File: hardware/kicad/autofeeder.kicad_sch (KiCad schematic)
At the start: 39 parts, among them J1 BATTERY, J2 MOTOR, J3 USB-C, J4 DBG, SW1_POWER1 Alps SKRPADE010, SW2_TIMER1 Alps SKRPADE010, SW3_MANUAL1 Alps SKRPADE010, SW4_SETTINGS1 Alps SKRPADE010, SW5_UP1 Alps SKRPADE010, SW6_DOWN1 Alps SKRPADE010, U1 ESP32-C6-Zero, U2 TP4056, U3 DW01A, U4 TPS63031DSKR, U5 DRV8871, U6 SN65HVD230, U8 FS8205A

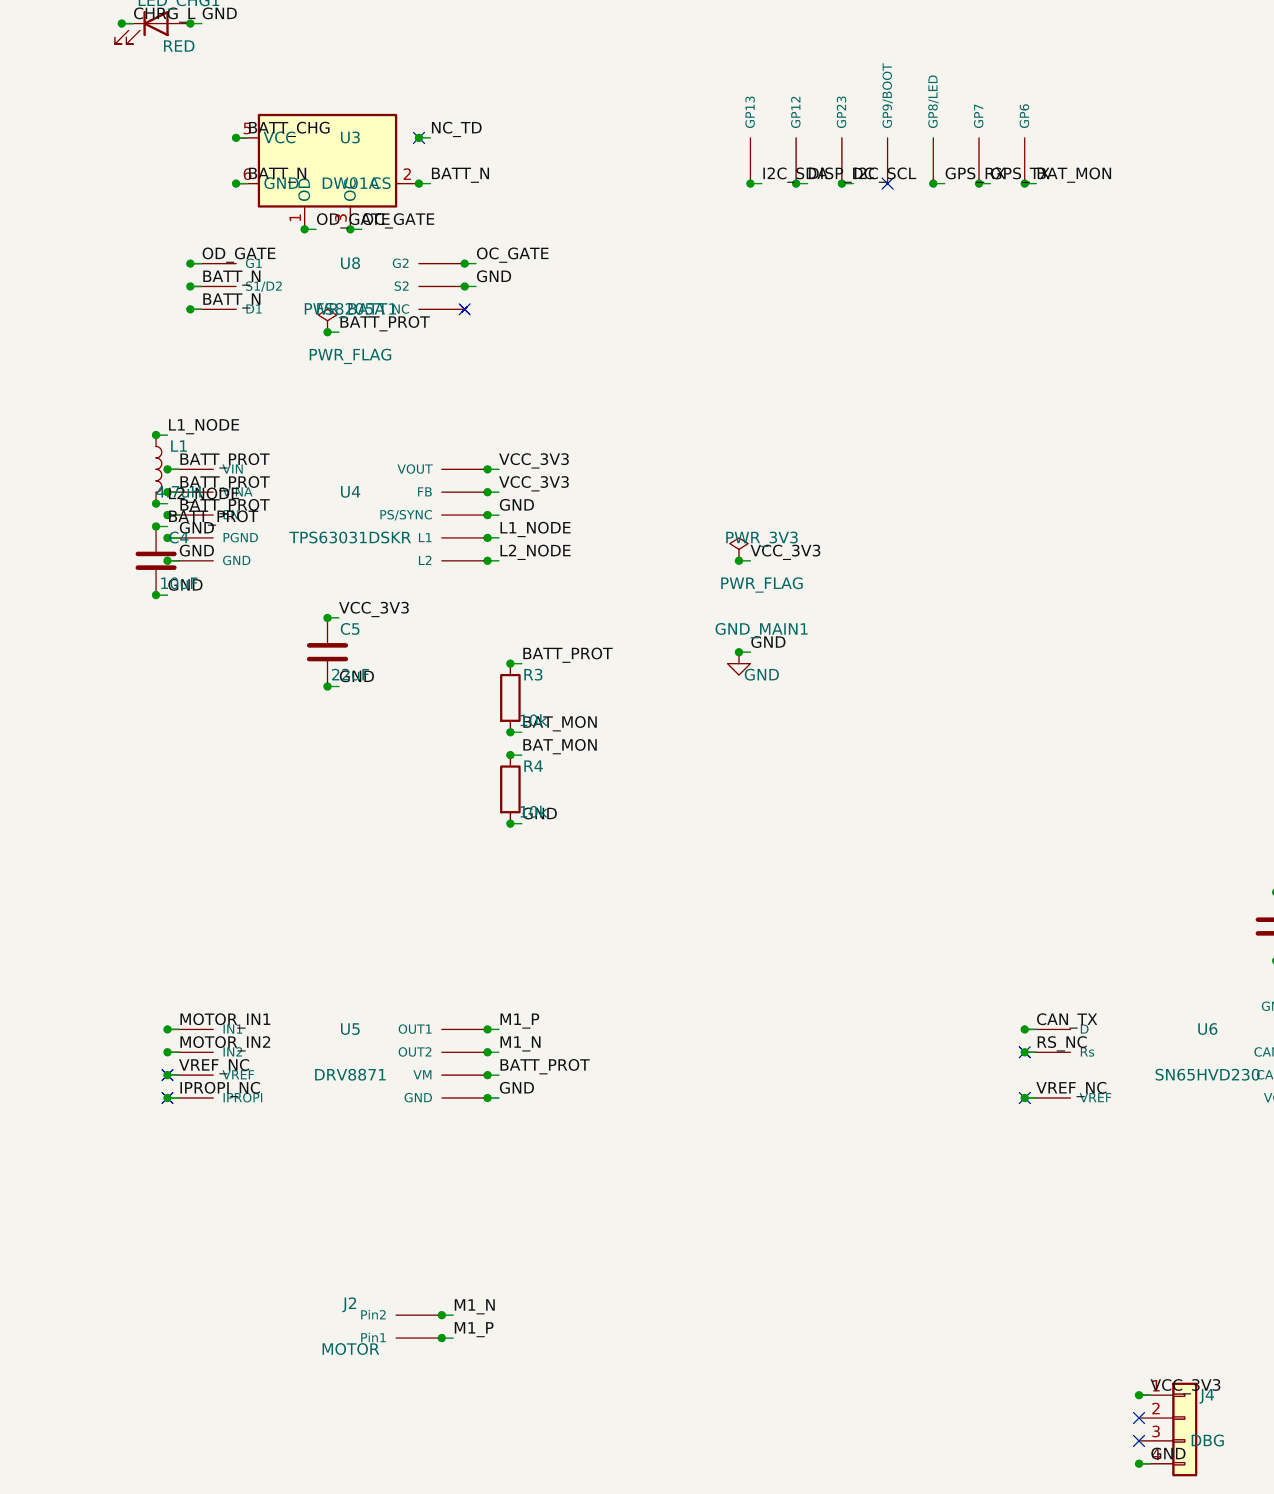
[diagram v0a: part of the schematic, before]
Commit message: Fix BATT_N unconnected net, migrate to 4-layer PCB, refresh fab outputs
- Add _pre_route_batt_n() to route BATT_N net (DW01A ↔ FS8205A protection ICs)
  via B.Cu segments + F.Cu through-via, eliminating the last unconnected net
- Update README power topology to include DW01A/FS8205A protection
- Update docs/bom.md: 2→4 layer count, remove stale bodge wire instructions,
  update DRC status to reflect 0 unconnected items
- Regenerate all fab outputs (gerbers, drill, BOM, CPL, DRC) for 4-layer board
- Add inner copper layers (In1.Cu, In2.Cu) to gerber set
- Add Wabo Labs logo footprint, display_sleep custom component
- Add MX1508 reference datasheets
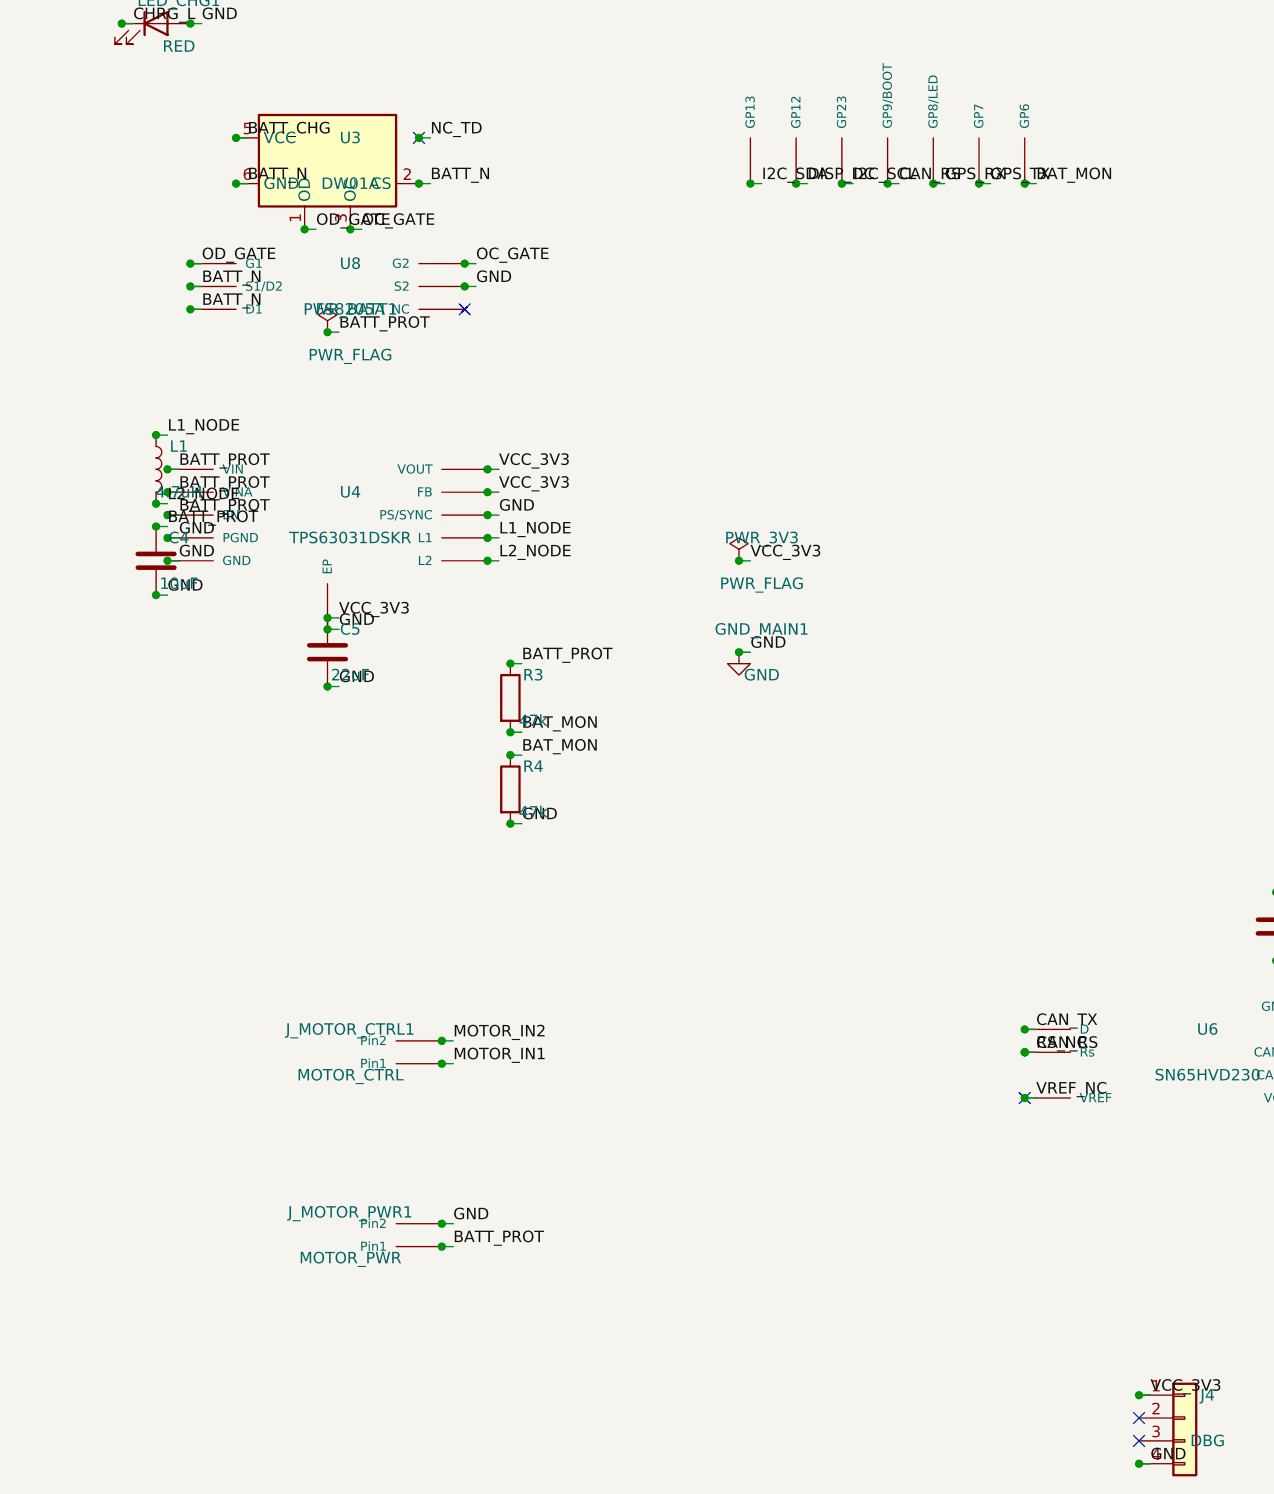
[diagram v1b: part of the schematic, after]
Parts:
- removed J2: MOTOR, Connector_JST:JST_XH_B2B-XH-A_1x02_P2.50mm_Vertical, symbol autofeeder:JST_XH_2P
- removed U5: DRV8871, Package_SO:SOIC-8_3.9x4.9mm_P1.27mm, symbol autofeeder:DRV8871
- added J_MOTOR_CTRL1: MOTOR_CTRL, Connector_JST:JST_XH_B2B-XH-A_1x02_P2.50mm_Vertical, symbol autofeeder:JST_XH_2P
- added J_MOTOR_PWR1: MOTOR_PWR, Connector_JST:JST_XH_B2B-XH-A_1x02_P2.50mm_Vertical, symbol autofeeder:JST_XH_2P
- R3, R4: value 10k -> 47k
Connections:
- net RS_NC is gone; now on net CAN_RS: U6.8 (Rs)
- net BATT_PROT: now also J_MOTOR_PWR1.1 (Pin1)
- net GND: now also U4.11 (EP), J_MOTOR_PWR1.2 (Pin2)
- net MOTOR_IN1: now also J_MOTOR_CTRL1.1 (Pin1)
- net MOTOR_IN2: now also J_MOTOR_CTRL1.2 (Pin2)
- net CAN_RS: now reaches U1.22 (GP9/BOOT)
- no-connect marks 16 -> 12
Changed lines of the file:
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@@
 	(junction (at 72.39 152.4) (diameter 0) (color 0 0 0 0))
 	(junction (at 72.39 154.94) (diameter 0) (color 0 0 0 0))
+	(junction (at 54.61 162.56) (diameter 0) (color 0 0 0 0))
 	(junction (at 35.56 140.97) (diameter 0) (color 0 0 0 0))
 	(junction (at 35.56 148.59) (diameter 0) (color 0 0 0 0))
@@
 	(junction (at 127 113.03) (diameter 0) (color 0 0 0 0))
 	(junction (at 121.92 113.03) (diameter 0) (color 0 0 0 0))
+	(junction (at 116.84 113.03) (diameter 0) (color 0 0 0 0))
 	(junction (at 144.78 55.88) (diameter 0) (color 0 0 0 0))
 	(junction (at 144.78 63.5) (diameter 0) (color 0 0 0 0))
 	(junction (at 144.78 66.04) (diameter 0) (color 0 0 0 0))
 	(junction (at 144.78 73.66) (diameter 0) (color 0 0 0 0))
-	(junction (at 36.83 207.01) (diameter 0) (color 0 0 0 0))
-	(junction (at 36.83 209.55) (diameter 0) (color 0 0 0 0))
-	(junction (at 72.39 207.01) (diameter 0) (color 0 0 0 0))
-	(junction (at 72.39 209.55) (diameter 0) (color 0 0 0 0))
-	(junction (at 36.83 212.09) (diameter 0) (color 0 0 0 0))
-	(junction (at 36.83 214.63) (diameter 0) (color 0 0 0 0))
-	(junction (at 72.39 212.09) (diameter 0) (color 0 0 0 0))
-	(junction (at 72.39 214.63) (diameter 0) (color 0 0 0 0))
-	(junction (at 67.31 241.3) (diameter 0) (color 0 0 0 0))
-	(junction (at 67.31 238.76) (diameter 0) (color 0 0 0 0))
+	(junction (at 67.31 210.82) (diameter 0) (color 0 0 0 0))
+	(junction (at 67.31 208.28) (diameter 0) (color 0 0 0 0))
+	(junction (at 67.31 231.14000000000001) (diameter 0) (color 0 0 0 0))
+	(junction (at 67.31 228.6) (diameter 0) (color 0 0 0 0))
 	(junction (at 132.08 207.01) (diameter 0) (color 0 0 0 0))
 	(junction (at 167.64000000000001 207.01) (diameter 0) (color 0 0 0 0))
@@
 	(junction (at 167.64000000000001 214.63) (diameter 0) (color 0 0 0 0))
 	(junction (at 167.64000000000001 204.47) (diameter 0) (color 0 0 0 0))
+	(junction (at 132.08 209.55) (diameter 0) (color 0 0 0 0))
 	(junction (at 170.18 205.74) (diameter 0) (color 0 0 0 0))
 	(junction (at 170.18 213.36) (diameter 0) (color 0 0 0 0))
@@
 	(no_connect (at 144.78 59.69))
 	(no_connect (at 144.78 62.230000000000004))
-	(no_connect (at 116.84 113.03))
-	(no_connect (at 36.83 212.09))
-	(no_connect (at 36.83 214.63))
 	(no_connect (at 132.08 214.63))
-	(no_connect (at 132.08 209.55))
 	(no_connect (at 144.78 250.19))
 	(no_connect (at 144.78 252.73))
@@
 	)
 	(wire
+		(pts (xy 54.61 162.56) (xy 55.88 162.56))
+		(stroke (width 0) (type solid))
+	)
+	(wire
 		(pts (xy 35.56 140.97) (xy 36.83 140.97))
 		(stroke (width 0) (type solid))
@@
 	)
 	(wire
+		(pts (xy 116.84 113.03) (xy 118.11 113.03))
+		(stroke (width 0) (type solid))
+	)
+	(wire
 		(pts (xy 144.78 55.88) (xy 146.05 55.88))
 		(stroke (width 0) (type solid))
@@
 	)
 	(wire
-		(pts (xy 36.83 207.01) (xy 38.1 207.01))
-		(stroke (width 0) (type solid))
-	)
-	(wire
-		(pts (xy 36.83 209.55) (xy 38.1 209.55))
-		(stroke (width 0) (type solid))
-	)
-	(wire
-		(pts (xy 72.39 207.01) (xy 73.66 207.01))
-		(stroke (width 0) (type solid))
-	)
-	(wire
-		(pts (xy 72.39 209.55) (xy 73.66 209.55))
-		(stroke (width 0) (type solid))
-	)
-	(wire
-		(pts (xy 36.83 212.09) (xy 38.1 212.09))
-		(stroke (width 0) (type solid))
-	)
-	(wire
-		(pts (xy 36.83 214.63) (xy 38.1 214.63))
-		(stroke (width 0) (type solid))
-	)
-	(wire
-		(pts (xy 72.39 212.09) (xy 73.66 212.09))
-		(stroke (width 0) (type solid))
-	)
-	(wire
-		(pts (xy 72.39 214.63) (xy 73.66 214.63))
-		(stroke (width 0) (type solid))
-	)
-	(wire
-		(pts (xy 67.31 241.3) (xy 68.58 241.3))
-		(stroke (width 0) (type solid))
-	)
-	(wire
-		(pts (xy 67.31 238.76) (xy 68.58 238.76))
+		(pts (xy 67.31 210.82) (xy 68.58 210.82))
+		(stroke (width 0) (type solid))
+	)
+	(wire
+		(pts (xy 67.31 208.28) (xy 68.58 208.28))
+		(stroke (width 0) (type solid))
+	)
+	(wire
+		(pts (xy 67.31 231.14000000000001) (xy 68.58 231.14000000000001))
+		(stroke (width 0) (type solid))
+	)
+	(wire
+		(pts (xy 67.31 228.6) (xy 68.58 228.6))
 		(stroke (width 0) (type solid))
 	)
@@
 		)
 	)
+	(label "GND"
+		(at 55.88 162.56 0)
+		(effects
+			(font (size 1.27 1.27))
+			(justify left bottom)
+		)
+	)
 	(label "L1_NODE"
 		(at 36.830000000000005 140.97 0)
@@
 		)
 	)
+	(label "CAN_RS"
+		(at 118.10999999999999 113.03 0)
+		(effects
+			(font (size 1.27 1.27))
+			(justify left bottom)
+		)
+	)
 	(label "VCC_3V3"
 		(at 146.05 55.879999999999995 0)
@@
 	)
 	(label "MOTOR_IN1"
-		(at 38.1 207.01000000000002 0)
+		(at 68.58 210.82000000000002 0)
 		(effects
 			(font (size 1.27 1.27))
@@
 	)
 	(label "MOTOR_IN2"
-		(at 38.1 209.55 0)
-		(effects
-			(font (size 1.27 1.27))
-			(justify left bottom)
-		)
-	)
-	(label "M1_P"
-		(at 73.66 207.01000000000002 0)
-		(effects
-			(font (size 1.27 1.27))
-			(justify left bottom)
-		)
-	)
-	(label "M1_N"
-		(at 73.66 209.55 0)
-		(effects
-			(font (size 1.27 1.27))
-			(justify left bottom)
-		)
-	)
-	(label "VREF_NC"
-		(at 38.1 212.09 0)
-		(effects
-			(font (size 1.27 1.27))
-			(justify left bottom)
-		)
-	)
-	(label "IPROPI_NC"
-		(at 38.1 214.63000000000002 0)
+		(at 68.58 208.28 0)
 		(effects
 			(font (size 1.27 1.27))
@@
 	)
 	(label "BATT_PROT"
-		(at 73.66 212.09 0)
-		(effects
-			(font (size 1.27 1.27))
-			(justify left bottom)
-		)
-	)
-	(label "GND"
-		(at 73.66 214.63000000000002 0)
-		(effects
-			(font (size 1.27 1.27))
-			(justify left bottom)
-		)
-	)
-	(label "M1_P"
-		(at 68.58 241.3 0)
-		(effects
-			(font (size 1.27 1.27))
-			(justify left bottom)
-		)
-	)
-	(label "M1_N"
-		(at 68.58 238.76 0)
+		(at 68.58 231.14000000000001 0)
+		(effects
+			(font (size 1.27 1.27))
+			(justify left bottom)
+		)
+	)
+	(label "GND"
+		(at 68.58 228.6 0)
 		(effects
 			(font (size 1.27 1.27))
@@
 	(label "GND"
 		(at 168.91000000000003 204.47 0)
+		(effects
+			(font (size 1.27 1.27))
+			(justify left bottom)
+		)
+	)
+	(label "CAN_RS"
+		(at 133.35000000000002 209.55 0)
 		(effects
 			(font (size 1.27 1.27))
@@
 			)
 		)
-		(property "Value" "10k"
+		(property "Value" "47k"
 			(at 77.47000000000001 172.72 0)
 			(effects
@@
 			)
 		)
-		(property "Value" "10k"
+		(property "Value" "47k"
 			(at 77.47000000000001 182.88 0)
 			(effects
@@
 	)
 	(symbol
-		(lib_id "autofeeder:DRV8871")
+		(lib_id "autofeeder:JST_XH_2P")
 		(at 54.61 209.55 0)
 		(unit 1)
@@
 		(in_bom yes)
 		(on_board yes)
-		(property "Reference" "U5"
+		(property "Reference" "J_MOTOR_CTRL1"
 			(at 57.15 207.01000000000002 0)
 			(effects
@@
 			)
 		)
-		(property "Value" "DRV8871"
+		(property "Value" "MOTOR_CTRL"
 			(at 57.15 212.09 0)
 			(effects
@@
 			)
 		)
-		(property "Footprint" "Package_SO:SOIC-8_3.9x4.9mm_P1.27mm"
+		(property "Footprint" "Connector_JST:JST_XH_B2B-XH-A_1x02_P2.50mm_Vertical"
 			(at 57.15 209.55 0)
 			(effects
@@
 		(instances
 			(project "autofeedermod"
-				(path "/00000000-0000-0000-0000-000000000000" (reference "U5") (unit 1))
+				(path "/00000000-0000-0000-0000-000000000000" (reference "J_MOTOR_CTRL1") (unit 1))
 			)
 		)
@@
 	(symbol
 		(lib_id "autofeeder:JST_XH_2P")
-		(at 54.61 240.03 0)
+		(at 54.61 229.87 0)
 		(unit 1)
 		(exclude_from_sim no)
 		(in_bom yes)
 		(on_board yes)
-		(property "Reference" "J2"
-			(at 57.15 237.49 0)
-			(effects
-				(font (size 1.27 1.27))
-			)
-		)
-		(property "Value" "MOTOR"
-			(at 57.15 242.57 0)
+		(property "Reference" "J_MOTOR_PWR1"
+			(at 57.15 227.33 0)
+			(effects
+				(font (size 1.27 1.27))
+			)
+		)
+		(property "Value" "MOTOR_PWR"
+			(at 57.15 232.41 0)
 			(effects
 				(font (size 1.27 1.27))
@@
 		)
 		(property "Footprint" "Connector_JST:JST_XH_B2B-XH-A_1x02_P2.50mm_Vertical"
-			(at 57.15 240.03 0)
+			(at 57.15 229.87 0)
 			(effects
 				(font (size 1.27 1.27))
@@
 		(instances
 			(project "autofeedermod"
-				(path "/00000000-0000-0000-0000-000000000000" (reference "J2") (unit 1))
-			)
-		)
+				(path "/00000000-0000-0000-0000-000000000000" (reference "J_MOTOR_PWR1") (unit 1))
+			)
+		)
